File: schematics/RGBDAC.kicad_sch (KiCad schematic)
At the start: 32 parts, among them U3 74LS245, U5 74LS245, U6 74LS32

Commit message: WIP
starting Page 2 : LSPC2
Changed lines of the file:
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@@
-    (stroke (width 0) (type default))
-  )
-  (bus (pts (xy 45.72 213.36) (xy 45.72 222.25))
     (stroke (width 0) (type default))
   )

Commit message: update readme
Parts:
- renumbered 6J to 6J1, 7J to 7J1, 9H to 9H2, 9K to 9K1, JAMMA to JAMMA5
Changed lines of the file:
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@@
   (symbol (lib_id "74xx:74LS273") (at 147.32 121.92 0) (unit 1)
     (in_bom yes) (on_board yes) (dnp no)
-    (property "Reference" "9H" (at 139.7 105.41 0)
+    (property "Reference" "9H2" (at 139.7 105.41 0)
       (effects (font (size 1.27 1.27)) (justify left))
     )
@@
       (project "MVS"
         (path "/8d0803ab-15ed-47a7-8dcb-ab27dc5b29c2/02d08188-cb7b-4e58-b274-9af0bca56e9a"
-          (reference "9H") (unit 1)
+          (reference "9H2") (unit 1)
         )
       )
@@
   (symbol (lib_id "74xx:74LS05") (at 203.2 149.86 0) (unit 2)
     (in_bom yes) (on_board yes) (dnp no)
-    (property "Reference" "9K" (at 200.66 144.78 0)
+    (property "Reference" "9K1" (at 200.66 144.78 0)
       (effects (font (size 1.27 1.27)))
     )
@@
       (project "MVS"
         (path "/8d0803ab-15ed-47a7-8dcb-ab27dc5b29c2/02d08188-cb7b-4e58-b274-9af0bca56e9a"
-          (reference "9K") (unit 2)
+          (reference "9K1") (unit 2)
         )
       )
@@
   (symbol (lib_id "74xx:74LS05") (at 203.2 205.74 0) (unit 3)
     (in_bom yes) (on_board yes) (dnp no)
-    (property "Reference" "9K" (at 200.66 200.66 0)
+    (property "Reference" "9K1" (at 200.66 200.66 0)
       (effects (font (size 1.27 1.27)))
     )
@@
       (project "MVS"
         (path "/8d0803ab-15ed-47a7-8dcb-ab27dc5b29c2/02d08188-cb7b-4e58-b274-9af0bca56e9a"
-          (reference "9K") (unit 3)
+          (reference "9K1") (unit 3)
         )
       )
@@
   (symbol (lib_id "74xx:74LS05") (at 203.2 137.16 0) (unit 5)
     (in_bom yes) (on_board yes) (dnp no)
-    (property "Reference" "9K" (at 200.66 132.08 0)
+    (property "Reference" "9K1" (at 200.66 132.08 0)
       (effects (font (size 1.27 1.27)))
     )
@@
       (project "MVS"
         (path "/8d0803ab-15ed-47a7-8dcb-ab27dc5b29c2/02d08188-cb7b-4e58-b274-9af0bca56e9a"
-          (reference "9K") (unit 5)
+          (reference "9K1") (unit 5)
         )
       )
@@
   (symbol (lib_id "74xx:74LS05") (at 203.2 100.33 0) (unit 1)
     (in_bom yes) (on_board yes) (dnp no)
-    (property "Reference" "9K" (at 200.66 95.25 0)
+    (property "Reference" "9K1" (at 200.66 95.25 0)
       (effects (font (size 1.27 1.27)))
     )
@@
       (project "MVS"
         (path "/8d0803ab-15ed-47a7-8dcb-ab27dc5b29c2/02d08188-cb7b-4e58-b274-9af0bca56e9a"
-          (reference "9K") (unit 1)
+          (reference "9K1") (unit 1)
         )
       )
@@
   (symbol (lib_id "Memory_RAM:KM62256CLP") (at 74.93 157.48 0) (unit 1)
     (in_bom yes) (on_board yes) (dnp no)
-    (property "Reference" "6J" (at 64.77 135.89 0)
+    (property "Reference" "6J1" (at 64.77 135.89 0)
       (effects (font (size 1.27 1.27)) (justify left))
     )
@@
       (project "MVS"
         (path "/8d0803ab-15ed-47a7-8dcb-ab27dc5b29c2/02d08188-cb7b-4e58-b274-9af0bca56e9a"
-          (reference "6J") (unit 1)
+          (reference "6J1") (unit 1)
         )
       )
@@
   (symbol (lib_id "Connector:Conn_01x01_Pin") (at 228.6 59.69 180) (unit 1)
     (in_bom yes) (on_board yes) (dnp no)
-    (property "Reference" "JAMMA" (at 227.965 55.4695 0)
+    (property "Reference" "JAMMA5" (at 227.965 55.4695 0)
       (effects (font (size 1.27 1.27)) hide)
     )
@@
       (project "MVS"
         (path "/8d0803ab-15ed-47a7-8dcb-ab27dc5b29c2/02d08188-cb7b-4e58-b274-9af0bca56e9a"
-          (reference "JAMMA") (unit 1)
+          (reference "JAMMA5") (unit 1)
         )
       )
@@
   (symbol (lib_id "74xx:74LS05") (at 203.2 193.04 0) (unit 4)
     (in_bom yes) (on_board yes) (dnp no)
-    (property "Reference" "9K" (at 200.66 187.96 0)
+    (property "Reference" "9K1" (at 200.66 187.96 0)
       (effects (font (size 1.27 1.27)))
     )
@@
       (project "MVS"
         (path "/8d0803ab-15ed-47a7-8dcb-ab27dc5b29c2/02d08188-cb7b-4e58-b274-9af0bca56e9a"
-          (reference "9K") (unit 4)
+          (reference "9K1") (unit 4)
         )
       )
@@
   (symbol (lib_id "74xx:74LS05") (at 203.2 87.63 0) (unit 6)
     (in_bom yes) (on_board yes) (dnp no)
-    (property "Reference" "9K" (at 200.66 82.55 0)
+    (property "Reference" "9K1" (at 200.66 82.55 0)
       (effects (font (size 1.27 1.27)))
     )
@@
       (project "MVS"
         (path "/8d0803ab-15ed-47a7-8dcb-ab27dc5b29c2/02d08188-cb7b-4e58-b274-9af0bca56e9a"
-          (reference "9K") (unit 6)
+          (reference "9K1") (unit 6)
         )
       )
@@
   (symbol (lib_id "Memory_RAM:KM62256CLP") (at 74.93 205.74 0) (unit 1)
     (in_bom yes) (on_board yes) (dnp no)
-    (property "Reference" "7J" (at 64.77 184.15 0)
+    (property "Reference" "7J1" (at 64.77 184.15 0)
       (effects (font (size 1.27 1.27)) (justify left))
     )
@@
       (project "MVS"
         (path "/8d0803ab-15ed-47a7-8dcb-ab27dc5b29c2/02d08188-cb7b-4e58-b274-9af0bca56e9a"
-          (reference "7J") (unit 1)
-        )
-      )
+          (reference "7J1") (unit 1)
+        )
+      )

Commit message: Complete pages 1-4
completion of pages 1 to 4
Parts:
- R10, R11, R12, R13, R14, R15, R16, R17, R18, R19, R20, R21, R22, R23, R24, R25, R5, R6, R7, R8, R9: symbol Device:R_Small_US -> Device:R
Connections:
- net R0: no longer R5.2
- net R1: no longer R6.2
- net R2: no longer R7.2
- net R3: no longer R8.2
- net R4: no longer R9.2
- net at JAMMA4.13 (Pin_13), R19.1, R20.1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: no longer R25.1
- now unconnected: JAMMA5.12 (Pin_12), R10.1, R11.1, R5.1, R6.1, R7.1, R8.1, R9.1

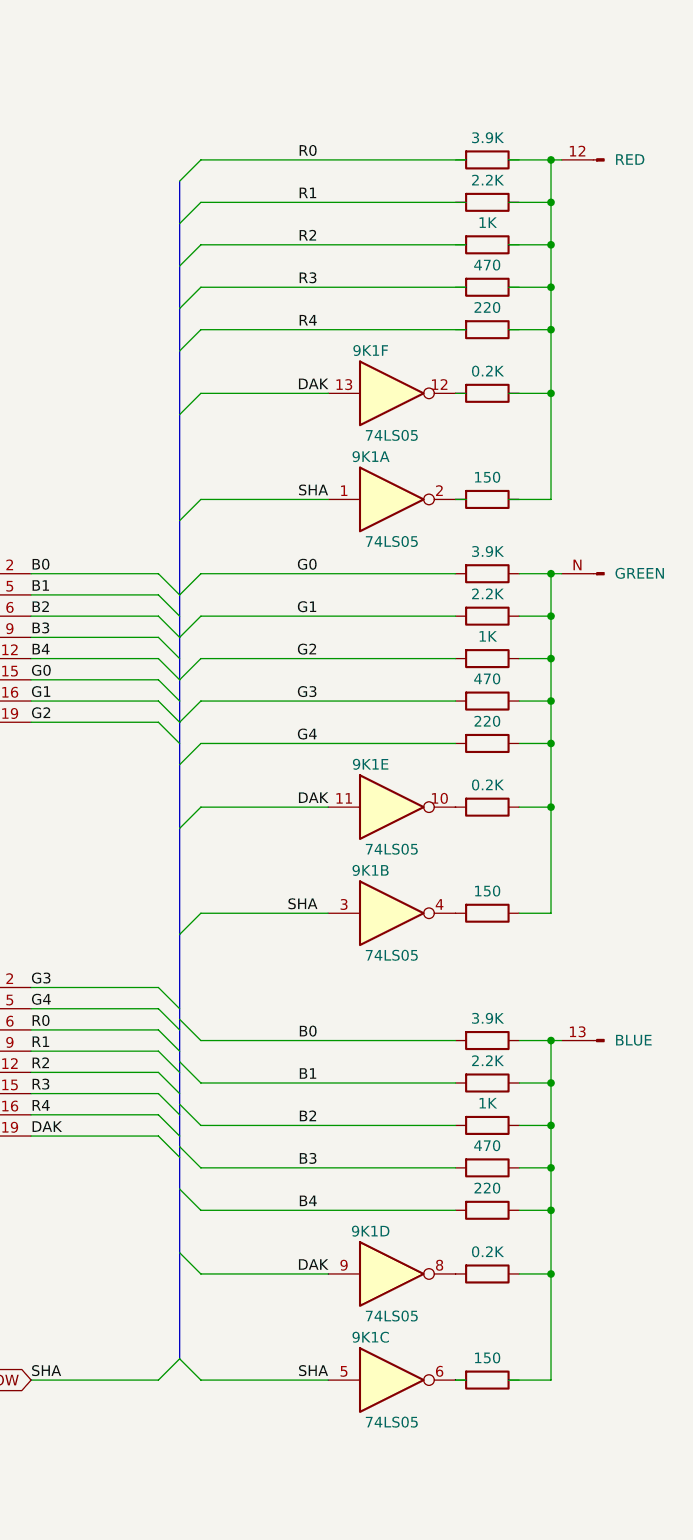
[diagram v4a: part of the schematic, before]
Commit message: Audio Amp + player's button LED & marquee + Coins Up + 45% raiser card connectors
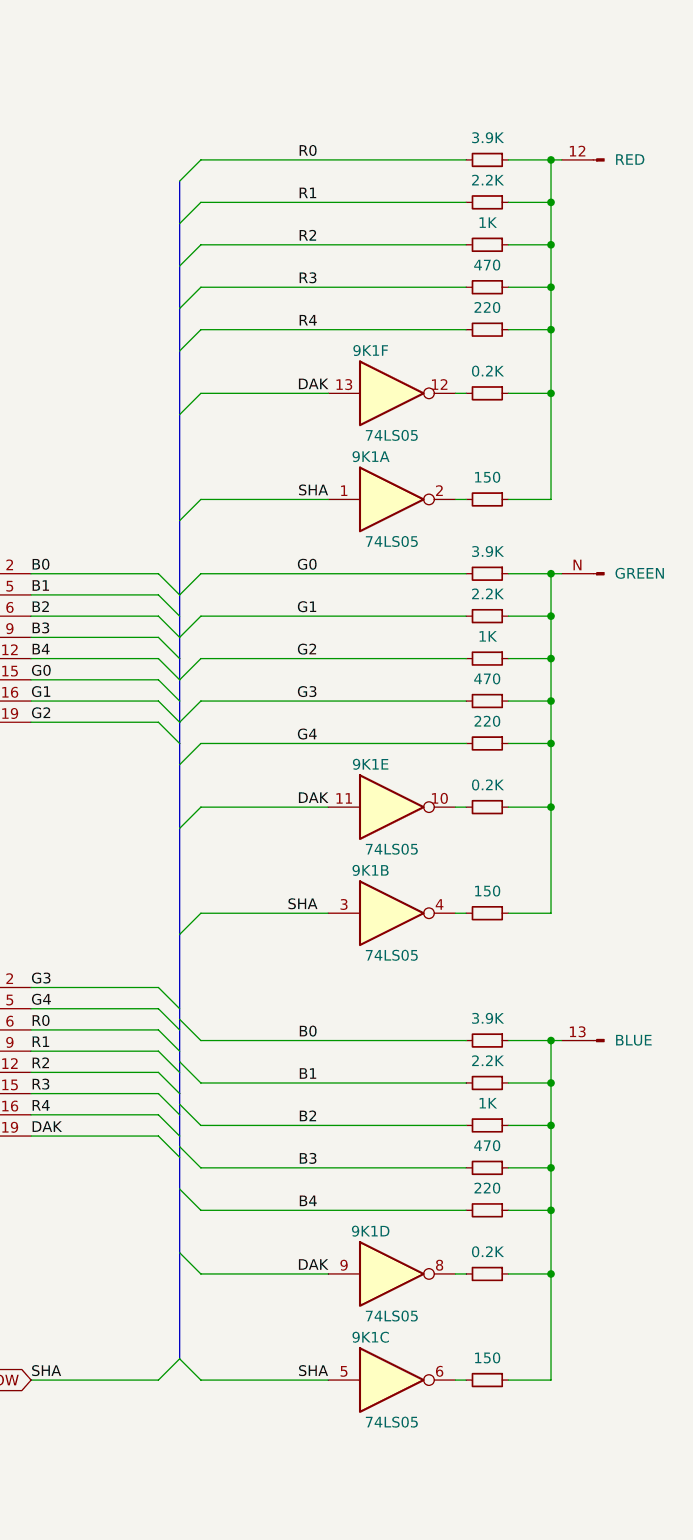
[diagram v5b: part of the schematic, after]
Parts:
- R10, R11, R12, R13, R14, R15, R16, R17, R18, R19, R20, R21, R22, R23, R24, R25, R5, R6, R7, R8, R9: symbol Device:R -> Device:R_Small
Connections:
- net R0: now also R5.2
- net R1: now also R6.2
- net R2: now also R7.2
- net R3: now also R8.2
- net R4: now also R9.2
- net at R6.1: now also JAMMA5.12 (Pin_12), R10.1, R11.1, R5.1, R7.1, R8.1, R9.1
- net at JAMMA4.13 (Pin_13), R19.1, R20.1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: now also R25.1

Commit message: typos
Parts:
- 9H1, 9H2, U3, U5: footprint (none) -> Package_DIP:DIP-20_W7.62mm
- 9K1, U6: footprint (none) -> Package_DIP:DIP-14_W7.62mm
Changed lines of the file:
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@@
     (comment 3 "Converted by Frater ")
     (comment 4 "NEO-GEO MVS MV1F")
+    (comment 9 "https://github.com/Neo-Geo-Hardwares/Schematics-MV1F")
   )
   (junction (at 55.88 133.35) (diameter 0) (color 0 0 0 0)
@@
       (effects (font (size 1.27 1.27)) (justify left))
     )
-    (property "Footprint" "" (at 72.39 82.55 0)
+    (property "Footprint" "Package_DIP:DIP-20_W7.62mm" (at 72.39 82.55 0)
       (effects (font (size 1.27 1.27)) hide)
     )
@@
       (effects (font (size 1.27 1.27)) (justify left))
     )
-    (property "Footprint" "" (at 147.32 121.92 0)
+    (property "Footprint" "Package_DIP:DIP-20_W7.62mm" (at 147.32 121.92 0)
       (effects (font (size 1.27 1.27)) hide)
     )
@@
       (effects (font (size 1.27 1.27)))
     )
-    (property "Footprint" "" (at 203.2 149.86 0)
+    (property "Footprint" "Package_DIP:DIP-14_W7.62mm" (at 203.2 149.86 0)
       (effects (font (size 1.27 1.27)) hide)
     )
@@
       (effects (font (size 1.27 1.27)))
     )
-    (property "Footprint" "" (at 203.2 205.74 0)
+    (property "Footprint" "Package_DIP:DIP-14_W7.62mm" (at 203.2 205.74 0)
       (effects (font (size 1.27 1.27)) hide)
     )
@@
       (effects (font (size 1.27 1.27)))
     )
-    (property "Footprint" "" (at 203.2 137.16 0)
+    (property "Footprint" "Package_DIP:DIP-14_W7.62mm" (at 203.2 137.16 0)
       (effects (font (size 1.27 1.27)) hide)
     )
@@
       (effects (font (size 1.27 1.27)) (justify left))
     )
-    (property "Footprint" "" (at 147.32 171.45 0)
+    (property "Footprint" "Package_DIP:DIP-20_W7.62mm" (at 147.32 171.45 0)
       (effects (font (size 1.27 1.27)) hide)
     )
@@
       (effects (font (size 1.27 1.27)))
     )
-    (property "Footprint" "" (at 203.2 100.33 0)
+    (property "Footprint" "Package_DIP:DIP-14_W7.62mm" (at 203.2 100.33 0)
       (effects (font (size 1.27 1.27)) hide)
     )
@@
       (effects (font (size 1.27 1.27)))
     )
-    (property "Footprint" "" (at 203.2 193.04 0)
+    (property "Footprint" "Package_DIP:DIP-14_W7.62mm" (at 203.2 193.04 0)
       (effects (font (size 1.27 1.27)) hide)
     )
@@
       (effects (font (size 1.27 1.27)))
     )
-    (property "Footprint" "" (at 203.2 87.63 0)
+    (property "Footprint" "Package_DIP:DIP-14_W7.62mm" (at 203.2 87.63 0)
       (effects (font (size 1.27 1.27)) hide)
     )
@@
       (effects (font (size 1.27 1.27)))
     )
-    (property "Footprint" "" (at 68.58 120.65 0)
+    (property "Footprint" "Package_DIP:DIP-14_W7.62mm" (at 68.58 120.65 0)
       (effects (font (size 1.27 1.27)) hide)
     )
@@
       (effects (font (size 1.27 1.27)) (justify left))
     )
-    (property "Footprint" "" (at 72.39 39.37 0)
+    (property "Footprint" "Package_DIP:DIP-20_W7.62mm" (at 72.39 39.37 0)
       (effects (font (size 1.27 1.27)) hide)
     )
